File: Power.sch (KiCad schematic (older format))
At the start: 11 parts, among them P1 24 pin MiniFit JR, SW1 SWITCH_INV

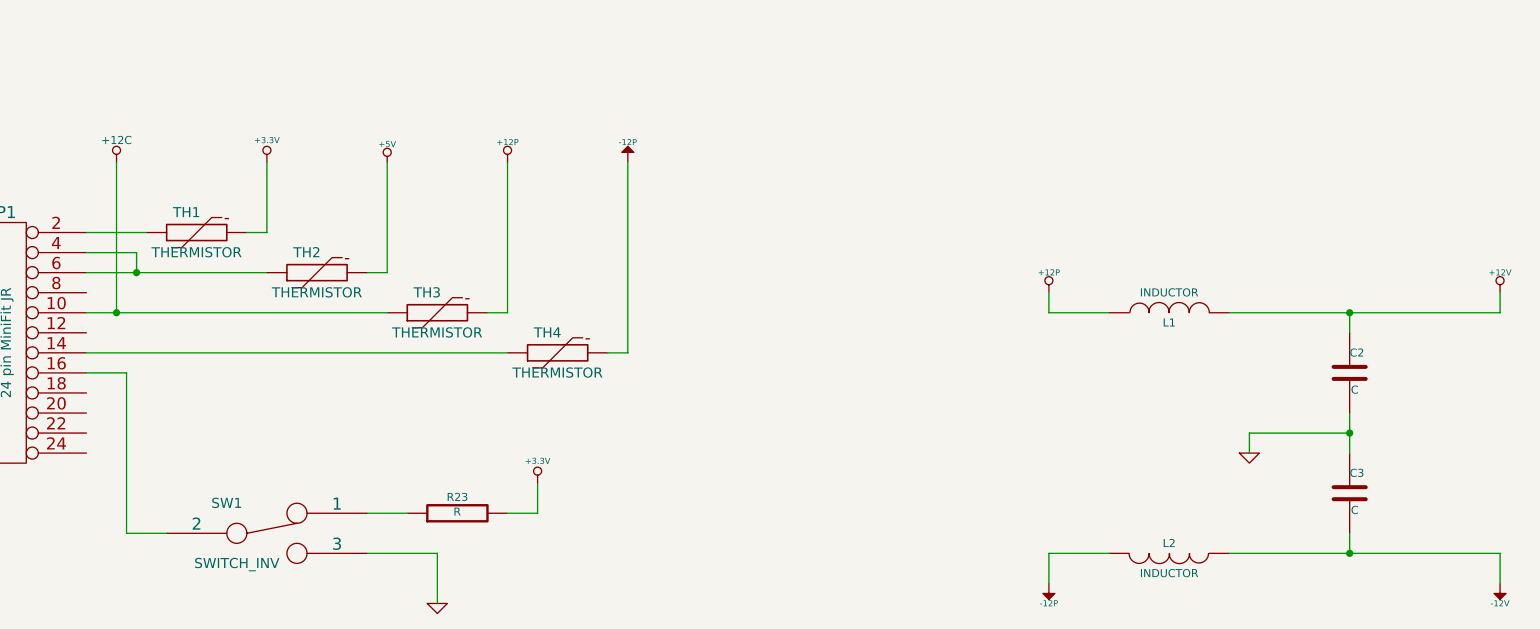
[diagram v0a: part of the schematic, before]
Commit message: Associating and Placing the Power Protection and Filtering Module
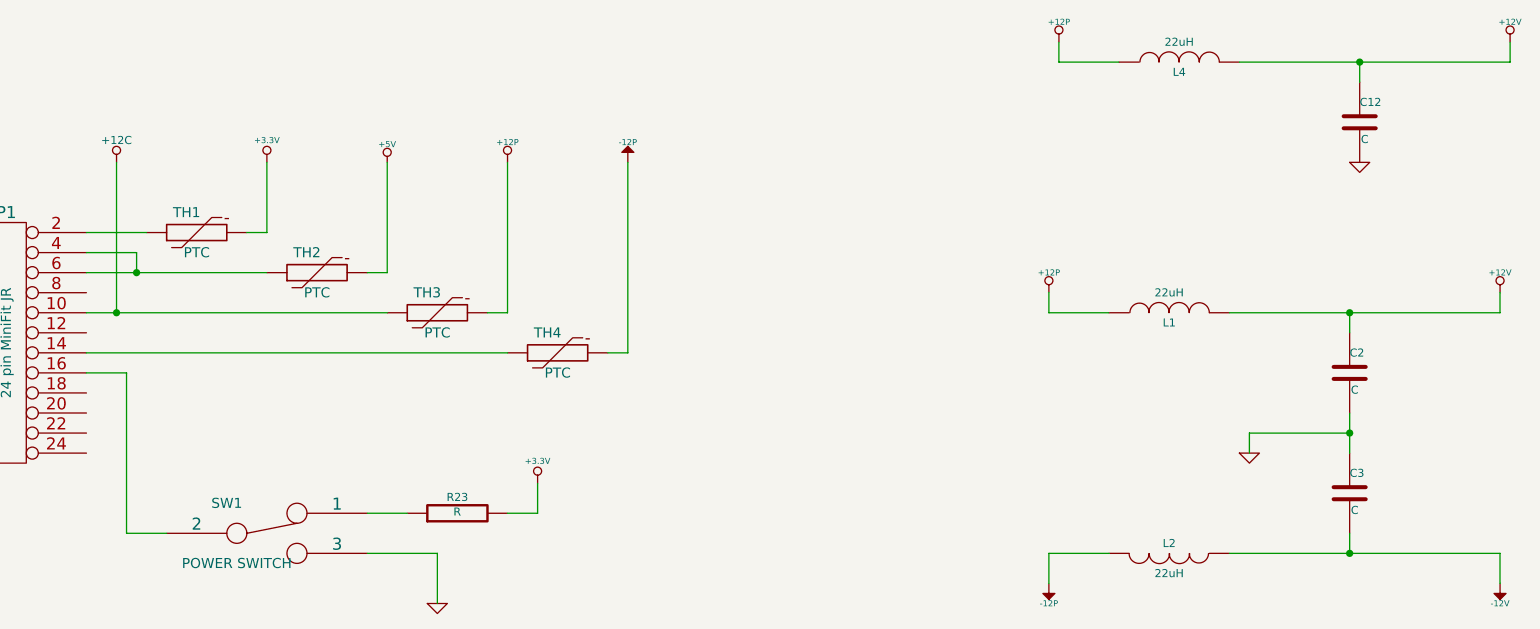
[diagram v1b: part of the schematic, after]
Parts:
- added C12: C, symbol C
- added L4: 22uH, symbol INDUCTOR
- L1, L2: value INDUCTOR -> 22uH; MFG Name (none) -> Bourns; MFG Part Number (none) -> CM322522-220KL
- SW1: value SWITCH_INV -> POWER SWITCH; MFG Name (none) -> C&K Components; MFG Part Number (none) -> OS102011MA1QN1
- TH1, TH2, TH3, TH4: value THERMISTOR -> PTC; MFG Name (none) -> TE Connectivity; MFG Part Number (none) -> MINISMDC050F-2
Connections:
- net +12P: now also L4.1
- net +12V: now also C12.1, L4.2
- net GND: now also C12.2
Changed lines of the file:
@@
 P 3700 3600
 F 0 "SW1" H 3500 3750 50  0000 C CNN
-F 1 "SWITCH_INV" H 3550 3450 50  0000 C CNN
+F 1 "POWER SWITCH" H 3550 3450 50  0000 C CNN
 F 2 "" H 3700 3600 60  0000 C CNN
 F 3 "" H 3700 3600 60  0000 C CNN
+F 4 "C&K Components" H 3700 3600 60  0001 C CNN "MFG Name"
+F 5 "OS102011MA1QN1" H 3700 3600 60  0001 C CNN "MFG Part Number"
 	1    3700 3600
 	1    0    0    -1
@@
 P 8200 2500
 F 0 "L1" V 8150 2500 40  0000 C CNN
-F 1 "INDUCTOR" V 8300 2500 40  0000 C CNN
+F 1 "22uH" V 8300 2500 40  0000 C CNN
 F 2 "" H 8200 2500 60  0000 C CNN
 F 3 "" H 8200 2500 60  0000 C CNN
+F 4 "Bourns" H 8200 2500 60  0001 C CNN "MFG Name"
+F 5 "CM322522-220KL" H 8200 2500 60  0001 C CNN "MFG Part Number"
 	1    8200 2500
 	0    -1   -1   0
@@
 P 8200 3700
 F 0 "L2" V 8150 3700 40  0000 C CNN
-F 1 "INDUCTOR" V 8300 3700 40  0000 C CNN
+F 1 "22uH" V 8300 3700 40  0000 C CNN
 F 2 "" H 8200 3700 60  0000 C CNN
 F 3 "" H 8200 3700 60  0000 C CNN
+F 4 "Bourns" H 8200 3700 60  0001 C CNN "MFG Name"
+F 5 "CM322522-220KL" H 8200 3700 60  0001 C CNN "MFG Part Number"
 	1    8200 3700
 	0    1    1    0
@@
 P 3350 2100
 F 0 "TH1" V 3450 2150 50  0000 C CNN
-F 1 "THERMISTOR" V 3250 2100 50  0000 C CNN
+F 1 "PTC" V 3250 2100 50  0000 C CNN
 F 2 "" H 3350 2100 60  0000 C CNN
 F 3 "" H 3350 2100 60  0000 C CNN
+F 4 "TE Connectivity" H 3350 2100 60  0001 C CNN "MFG Name"
+F 5 "MINISMDC050F-2" H 3350 2100 60  0001 C CNN "MFG Part Number"
 	1    3350 2100
 	0    -1   -1   0
@@
 P 3950 2300
 F 0 "TH2" V 4050 2350 50  0000 C CNN
-F 1 "THERMISTOR" V 3850 2300 50  0000 C CNN
+F 1 "PTC" V 3850 2300 50  0000 C CNN
 F 2 "" H 3950 2300 60  0000 C CNN
 F 3 "" H 3950 2300 60  0000 C CNN
+F 4 "TE Connectivity" H 3950 2300 60  0001 C CNN "MFG Name"
+F 5 "MINISMDC050F-2" H 3950 2300 60  0001 C CNN "MFG Part Number"
 	1    3950 2300
 	0    -1   -1   0
@@
 P 4550 2500
 F 0 "TH3" V 4650 2550 50  0000 C CNN
-F 1 "THERMISTOR" V 4450 2500 50  0000 C CNN
+F 1 "PTC" V 4450 2500 50  0000 C CNN
 F 2 "" H 4550 2500 60  0000 C CNN
 F 3 "" H 4550 2500 60  0000 C CNN
+F 4 "TE Connectivity" H 4550 2500 60  0001 C CNN "MFG Name"
+F 5 "MINISMDC050F-2" H 4550 2500 60  0001 C CNN "MFG Part Number"
 	1    4550 2500
 	0    -1   -1   0
@@
 P 5150 2700
 F 0 "TH4" V 5250 2750 50  0000 C CNN
-F 1 "THERMISTOR" V 5050 2700 50  0000 C CNN
+F 1 "PTC" V 5050 2700 50  0000 C CNN
 F 2 "" H 5150 2700 60  0000 C CNN
 F 3 "" H 5150 2700 60  0000 C CNN
+F 4 "TE Connectivity" H 5150 2700 60  0001 C CNN "MFG Name"
+F 5 "MINISMDC050F-2" H 5150 2700 60  0001 C CNN "MFG Part Number"
 	1    5150 2700
 	0    -1   -1   0
 $EndComp
+$Comp
+L +12P #PWR034
+U 1 1 530B10FD
+P 7650 1150
+F 0 "#PWR034" H 7650 1120 30  0001 C CNN
+F 1 "+12P" H 7650 1250 30  0000 C CNN
+F 2 "" H 7650 1150 60  0000 C CNN
+F 3 "" H 7650 1150 60  0000 C CNN
+	1    7650 1150
+	1    0    0    -1
+$EndComp
+$Comp
+L INDUCTOR L4
+U 1 1 530B1105
+P 8250 1250
+F 0 "L4" V 8200 1250 40  0000 C CNN
+F 1 "22uH" V 8350 1250 40  0000 C CNN
+F 2 "" H 8250 1250 60  0000 C CNN
+F 3 "" H 8250 1250 60  0000 C CNN
+F 4 "Bourns" H 8250 1250 60  0001 C CNN "MFG Name"
+F 5 "CM322522-220KL" H 8250 1250 60  0001 C CNN "MFG Part Number"
+	1    8250 1250
+	0    -1   -1   0
+$EndComp
+$Comp
+L C C12
+U 1 1 530B110B
+P 9150 1550
+F 0 "C12" H 9150 1650 40  0000 L CNN
+F 1 "C" H 9156 1465 40  0000 L CNN
+F 2 "" H 9188 1400 30  0000 C CNN
+F 3 "" H 9150 1550 60  0000 C CNN
+	1    9150 1550
+	1    0    0    -1
+$EndComp
+Wire Wire Line
+	9150 1350 9150 1250
+Wire Wire Line
+	8550 1250 9900 1250
+Wire Wire Line
+	7650 1150 7650 1250
+Wire Wire Line
+	7650 1250 7950 1250
+$Comp
+L +12V #PWR035
+U 1 1 530B1115
+P 9900 1150
+F 0 "#PWR035" H 9900 1100 20  0001 C CNN
+F 1 "+12V" H 9900 1250 30  0000 C CNN
+F 2 "" H 9900 1150 60  0000 C CNN
+F 3 "" H 9900 1150 60  0000 C CNN
+	1    9900 1150
+	1    0    0    -1
+$EndComp
+Wire Wire Line
+	9900 1250 9900 1150
+Connection ~ 9150 1250
+$Comp
+L GND #PWR036
+U 1 1 530B111D
+P 9150 1750
+F 0 "#PWR036" H 9150 1750 30  0001 C CNN
+F 1 "GND" H 9150 1680 30  0001 C CNN
+F 2 "" H 9150 1750 60  0000 C CNN
+F 3 "" H 9150 1750 60  0000 C CNN
+	1    9150 1750
+	1    0    0    -1
+$EndComp
 $EndSCHEMATC

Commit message: Merge CE BenchBudEE commit 00937c39d96b9ebb1b0292c11cc231788ab24edd
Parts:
- removed C12: C, symbol C
- removed L4: 22uH, symbol INDUCTOR
- removed R23: R, symbol R
- added C4: C, ~, symbol C
- added L3: CM322522-220KL, ~, symbol INDUCTOR
- added R14: R, ~, symbol R
- C2, C3: footprint (none) -> ~
- L1, L2: value 22uH -> CM322522-220KL; footprint (none) -> ~; MFG Name Bourns -> Bournes
- P1: value 24 pin MiniFit JR -> 24 Pin MiniFit JR
- SW1: value POWER SWITCH -> Power Switch; footprint (none) -> ~
- TH1, TH2, TH3, TH4: value PTC -> MINISMDC050F-2; footprint (none) -> ~
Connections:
- net +12P: now also L3.1; no longer L1.1
- net +12V: now also C3.1, L3.2; no longer C2.1, L1.2
- net +3.3V: now also R14.2
- net +5V: now also C2.1, L1.2; no longer TH2.2
- net -12V: now also C4.2; no longer C3.2
- net GND: now also C3.2, C4.1; no longer C3.1
- net at P1.12 (P12): now also P1.2 (P2), TH1.1
- net at SW1.1: now also R14.1
- new net +5P: L1.1, TH2.2

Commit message: Layout Work Session 6
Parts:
- added TP1: CONN_1, symbol CONN_1
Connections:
- net GND: now also TP1.1
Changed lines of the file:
@@
 $EndComp
 $Comp
-L GND #PWR045
+L GND #PWR046
 U 1 1 523DFA76
 P 1400 1850
-F 0 "#PWR045" H 1400 1850 30  0001 C CNN
+F 0 "#PWR046" H 1400 1850 30  0001 C CNN
 F 1 "GND" H 1400 1780 30  0001 C CNN
 F 2 "" H 1400 1850 60  0000 C CNN
@@
 	5500 1900 5500 1150
 $Comp
-L +12P #PWR046
+L +12P #PWR047
 U 1 1 523DFB91
 P 5500 1150
-F 0 "#PWR046" H 5500 1120 30  0001 C CNN
+F 0 "#PWR047" H 5500 1120 30  0001 C CNN
 F 1 "+12P" H 5500 1250 30  0000 C CNN
 F 2 "" H 5500 1150 60  0000 C CNN
@@
 $EndComp
 $Comp
-L -12P #PWR047
+L -12P #PWR048
 U 1 1 523E04D8
 P 6100 1150
-F 0 "#PWR047" H 6100 1280 20  0001 C CNN
+F 0 "#PWR048" H 6100 1280 20  0001 C CNN
 F 1 "-12P" H 6100 1250 30  0000 C CNN
 F 2 "" H 6100 1150 60  0000 C CNN
@@
 	4800 3200 4800 3450
 $Comp
-L GND #PWR048
+L GND #PWR049
 U 1 1 523E08C4
 P 4800 3450
-F 0 "#PWR048" H 4800 3450 30  0001 C CNN
+F 0 "#PWR049" H 4800 3450 30  0001 C CNN
 F 1 "GND" H 4800 3380 30  0001 C CNN
 F 2 "" H 4800 3450 60  0000 C CNN
@@
 	5650 3000 5650 2750
 $Comp
-L +3.3V #PWR049
+L +3.3V #PWR050
 U 1 1 523E0910
 P 5650 2750
-F 0 "#PWR049" H 5650 2710 30  0001 C CNN
+F 0 "#PWR050" H 5650 2710 30  0001 C CNN
 F 1 "+3.3V" H 5650 2860 30  0000 C CNN
 F 2 "" H 5650 2750 60  0000 C CNN
@@
 $EndComp
 $Comp
-L +12P #PWR050
+L +12P #PWR051
 U 1 1 523E0C76
 P 8000 2250
-F 0 "#PWR050" H 8000 2220 30  0001 C CNN
+F 0 "#PWR051" H 8000 2220 30  0001 C CNN
 F 1 "+12P" H 8000 2350 30  0000 C CNN
 F 2 "" H 8000 2250 60  0000 C CNN
@@
 $EndComp
 $Comp
-L -12P #PWR051
+L -12P #PWR052
 U 1 1 523E0C7C
 P 8000 3800
-F 0 "#PWR051" H 8000 3930 20  0001 C CNN
+F 0 "#PWR052" H 8000 3930 20  0001 C CNN
 F 1 "-12P" H 8000 3900 30  0000 C CNN
 F 2 "" H 8000 3800 60  0000 C CNN
@@
 $EndComp
 $Comp
-L GND #PWR052
+L GND #PWR053
 U 1 1 523E0C82
 P 9000 3200
-F 0 "#PWR052" H 9000 3200 30  0001 C CNN
+F 0 "#PWR053" H 9000 3200 30  0001 C CNN
 F 1 "GND" H 9000 3130 30  0001 C CNN
 F 2 "" H 9000 3200 60  0000 C CNN
@@
 Connection ~ 9450 3050
 $Comp
-L -12V #PWR053
+L -12V #PWR054
 U 1 1 523E0DD3
 P 10350 3800
-F 0 "#PWR053" H 10350 3930 20  0001 C CNN
+F 0 "#PWR054" H 10350 3930 20  0001 C CNN
 F 1 "-12V" H 10350 3900 30  0000 C CNN
 F 2 "" H 10350 3800 60  0000 C CNN
@@
 Connection ~ 9450 2450
 $Comp
-L +12V #PWR054
+L +12V #PWR055
 U 1 1 523E0E37
 P 10350 2200
-F 0 "#PWR054" H 10350 2150 20  0001 C CNN
+F 0 "#PWR055" H 10350 2150 20  0001 C CNN
 F 1 "+12V" H 10350 2300 30  0000 C CNN
 F 2 "" H 10350 2200 60  0000 C CNN
@@
 Connection ~ 3450 1900
 $Comp
-L +12C #PWR055
+L +12C #PWR056
 U 1 1 52438F0D
 P 3450 1150
-F 0 "#PWR055" H 3450 1120 30  0001 C CNN
+F 0 "#PWR056" H 3450 1120 30  0001 C CNN
 F 1 "+12C" H 3450 1260 40  0000 C CNN
 F 2 "~" H 3450 1150 60  0000 C CNN
@@
 $EndComp
 $Comp
-L GND #PWR056
+L GND #PWR057
 U 1 1 524502FC
 P 9400 1650
-F 0 "#PWR056" H 9400 1650 30  0001 C CNN
+F 0 "#PWR057" H 9400 1650 30  0001 C CNN
 F 1 "GND" H 9400 1580 30  0001 C CNN
 F 2 "" H 9400 1650 60  0000 C CNN
@@
 $EndComp
 $Comp
-L +5V #PWR057
+L +5V #PWR058
 U 1 1 524503B6
 P 10300 650
-F 0 "#PWR057" H 10300 740 20  0001 C CNN
+F 0 "#PWR058" H 10300 740 20  0001 C CNN
 F 1 "+5V" H 10300 740 30  0000 C CNN
 F 2 "~" H 10300 650 60  0000 C CNN
@@
 $EndComp
 $Comp
-L +3.3V #PWR058
+L +3.3V #PWR059
 U 1 1 526E168C
 P 4400 1150
-F 0 "#PWR058" H 4400 1110 30  0001 C CNN
+F 0 "#PWR059" H 4400 1110 30  0001 C CNN
 F 1 "+3.3V" H 4400 1260 30  0000 C CNN
 F 2 "" H 4400 1150 60  0000 C CNN
@@
 	3550 2000 3550 1500
 Connection ~ 3550 1500
+$Comp
+L CONN_1 TP1
+U 1 1 53148E2B
+P 6775 4025
+F 0 "TP1" H 6855 4025 40  0000 L CNN
+F 1 "CONN_1" H 6775 4080 30  0001 C CNN
+F 2 "" H 6775 4025 60  0000 C CNN
+F 3 "" H 6775 4025 60  0000 C CNN
+	1    6775 4025
+	-1   0    0    1
+$EndComp
+$Comp
+L GND #PWR060
+U 1 1 53148E56
+P 7100 4125
+F 0 "#PWR060" H 7100 4125 30  0001 C CNN
+F 1 "GND" H 7100 4055 30  0001 C CNN
+F 2 "" H 7100 4125 60  0000 C CNN
+F 3 "" H 7100 4125 60  0000 C CNN
+	1    7100 4125
+	1    0    0    -1
+$EndComp
+Wire Wire Line
+	7100 4125 7100 4025
+Wire Wire Line
+	7100 4025 6925 4025
 $EndSCHEMATC

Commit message: Layout Work Session 6
Pulled from CE
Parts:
- added JP1, JP2, JP3, JP4: JUMPER, ~, symbol JUMPER
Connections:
- net GND: now also JP1.1, JP2.1, JP3.1, JP4.1
- new net AGND: JP1.2
- new net GND_LED: JP3.2
- new net GND_PWR: JP2.2
- new net GND_RELAY: JP4.2
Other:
- note added: "Star Point"
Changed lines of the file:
@@
-EESchema Schematic File Version 2
+EESchema Schematic File Version 2  date 11/10/2013 9:27:17 PM
 LIBS:power
 LIBS:device
@@
 LIBS:valves
 LIBS:BenchBuddy
-LIBS:arduino_shieldsNCL
 LIBS:BenchBuddy-cache
-EELAYER 24 0
+EELAYER 27 0
 EELAYER END
 $Descr A4 11693 8268
@@
 Sheet 9 9
 Title ""
-Date "2 nov 2013"
+Date "11 nov 2013"
 Rev ""
 Comp ""
@@
 $EndComp
 $Comp
-L GND #PWR046
+L GND #PWR51
 U 1 1 523DFA76
 P 1400 1850
-F 0 "#PWR046" H 1400 1850 30  0001 C CNN
+F 0 "#PWR51" H 1400 1850 30  0001 C CNN
 F 1 "GND" H 1400 1780 30  0001 C CNN
 F 2 "" H 1400 1850 60  0000 C CNN
@@
 	5500 1900 5500 1150
 $Comp
-L +12P #PWR047
+L +12P #PWR57
 U 1 1 523DFB91
 P 5500 1150
-F 0 "#PWR047" H 5500 1120 30  0001 C CNN
+F 0 "#PWR57" H 5500 1120 30  0001 C CNN
 F 1 "+12P" H 5500 1250 30  0000 C CNN
 F 2 "" H 5500 1150 60  0000 C CNN
@@
 $EndComp
 $Comp
-L -12P #PWR048
+L -12P #PWR59
 U 1 1 523E04D8
 P 6100 1150
-F 0 "#PWR048" H 6100 1280 20  0001 C CNN
+F 0 "#PWR59" H 6100 1280 20  0001 C CNN
 F 1 "-12P" H 6100 1250 30  0000 C CNN
 F 2 "" H 6100 1150 60  0000 C CNN
@@
 	4800 3200 4800 3450
 $Comp
-L GND #PWR049
+L GND #PWR54
 U 1 1 523E08C4
 P 4800 3450
-F 0 "#PWR049" H 4800 3450 30  0001 C CNN
+F 0 "#PWR54" H 4800 3450 30  0001 C CNN
 F 1 "GND" H 4800 3380 30  0001 C CNN
 F 2 "" H 4800 3450 60  0000 C CNN
@@
 	5650 3000 5650 2750
 $Comp
-L +3.3V #PWR050
+L +3.3V #PWR58
 U 1 1 523E0910
 P 5650 2750
-F 0 "#PWR050" H 5650 2710 30  0001 C CNN
+F 0 "#PWR58" H 5650 2710 30  0001 C CNN
 F 1 "+3.3V" H 5650 2860 30  0000 C CNN
 F 2 "" H 5650 2750 60  0000 C CNN
@@
 $EndComp
 $Comp
-L +12P #PWR051
+L +12P #PWR66
 U 1 1 523E0C76
 P 8000 2250
-F 0 "#PWR051" H 8000 2220 30  0001 C CNN
+F 0 "#PWR66" H 8000 2220 30  0001 C CNN
 F 1 "+12P" H 8000 2350 30  0000 C CNN
 F 2 "" H 8000 2250 60  0000 C CNN
@@
 $EndComp
 $Comp
-L -12P #PWR052
+L -12P #PWR67
 U 1 1 523E0C7C
 P 8000 3800
-F 0 "#PWR052" H 8000 3930 20  0001 C CNN
+F 0 "#PWR67" H 8000 3930 20  0001 C CNN
 F 1 "-12P" H 8000 3900 30  0000 C CNN
 F 2 "" H 8000 3800 60  0000 C CNN
@@
 $EndComp
 $Comp
-L GND #PWR053
+L GND #PWR68
 U 1 1 523E0C82
 P 9000 3200
-F 0 "#PWR053" H 9000 3200 30  0001 C CNN
+F 0 "#PWR68" H 9000 3200 30  0001 C CNN
 F 1 "GND" H 9000 3130 30  0001 C CNN
 F 2 "" H 9000 3200 60  0000 C CNN
@@
 Connection ~ 9450 3050
 $Comp
-L -12V #PWR054
+L -12V #PWR72
 U 1 1 523E0DD3
 P 10350 3800
-F 0 "#PWR054" H 10350 3930 20  0001 C CNN
+F 0 "#PWR72" H 10350 3930 20  0001 C CNN
 F 1 "-12V" H 10350 3900 30  0000 C CNN
 F 2 "" H 10350 3800 60  0000 C CNN
@@
 Connection ~ 9450 2450
 $Comp
-L +12V #PWR055
+L +12V #PWR71
 U 1 1 523E0E37
 P 10350 2200
-F 0 "#PWR055" H 10350 2150 20  0001 C CNN
+F 0 "#PWR71" H 10350 2150 20  0001 C CNN
 F 1 "+12V" H 10350 2300 30  0000 C CNN
 F 2 "" H 10350 2200 60  0000 C CNN
@@
 Connection ~ 3450 1900
 $Comp
-L +12C #PWR056
+L +12C #PWR52
 U 1 1 52438F0D
 P 3450 1150
-F 0 "#PWR056" H 3450 1120 30  0001 C CNN
+F 0 "#PWR52" H 3450 1120 30  0001 C CNN
 F 1 "+12C" H 3450 1260 40  0000 C CNN
 F 2 "~" H 3450 1150 60  0000 C CNN
@@
 $EndComp
 $Comp
-L GND #PWR057
+L GND #PWR69
 U 1 1 524502FC
 P 9400 1650
-F 0 "#PWR057" H 9400 1650 30  0001 C CNN
+F 0 "#PWR69" H 9400 1650 30  0001 C CNN
 F 1 "GND" H 9400 1580 30  0001 C CNN
 F 2 "" H 9400 1650 60  0000 C CNN
@@
 Connection ~ 9400 900
 $Comp
-L +5P #PWR58
+L +5P #PWR56
 U 1 1 52450355
 P 4900 1150
-F 0 "#PWR58" H 4900 1280 20  0001 C CNN
+F 0 "#PWR56" H 4900 1280 20  0001 C CNN
 F 1 "+5P" H 4900 1250 30  0000 C CNN
 F 2 "~" H 4900 1150 60  0000 C CNN
@@
 $EndComp
 $Comp
-L +5P #PWR62
+L +5P #PWR65
 U 1 1 52450371
 P 7950 700
-F 0 "#PWR62" H 7950 830 20  0001 C CNN
+F 0 "#PWR65" H 7950 830 20  0001 C CNN
 F 1 "+5P" H 7950 800 30  0000 C CNN
 F 2 "~" H 7950 700 60  0000 C CNN
@@
 $EndComp
 $Comp
-L +5V #PWR058
+L +5V #PWR70
 U 1 1 524503B6
 P 10300 650
-F 0 "#PWR058" H 10300 740 20  0001 C CNN
+F 0 "#PWR70" H 10300 740 20  0001 C CNN
 F 1 "+5V" H 10300 740 30  0000 C CNN
 F 2 "~" H 10300 650 60  0000 C CNN
@@
 $EndComp
 $Comp
-L +3.3V #PWR059
+L +3.3V #PWR53
 U 1 1 526E168C
 P 4400 1150
-F 0 "#PWR059" H 4400 1110 30  0001 C CNN
+F 0 "#PWR53" H 4400 1110 30  0001 C CNN
 F 1 "+3.3V" H 4400 1260 30  0000 C CNN
 F 2 "" H 4400 1150 60  0000 C CNN
@@
 $Comp
 L CONN_1 TP1
-U 1 1 53148E2B
-P 6775 4025
-F 0 "TP1" H 6855 4025 40  0000 L CNN
-F 1 "CONN_1" H 6775 4080 30  0001 C CNN
-F 2 "" H 6775 4025 60  0000 C CNN
-F 3 "" H 6775 4025 60  0000 C CNN
-	1    6775 4025
+U 1 1 527EFE16
+P 5800 5400
+F 0 "TP1" H 5880 5400 40  0000 L CNN
+F 1 "CONN_1" H 5800 5455 30  0001 C CNN
+F 2 "" H 5800 5400 60  0000 C CNN
+F 3 "" H 5800 5400 60  0000 C CNN
+	1    5800 5400
 	-1   0    0    1
 $EndComp
 $Comp
-L GND #PWR060
-U 1 1 53148E56
-P 7100 4125
-F 0 "#PWR060" H 7100 4125 30  0001 C CNN
-F 1 "GND" H 7100 4055 30  0001 C CNN
-F 2 "" H 7100 4125 60  0000 C CNN
-F 3 "" H 7100 4125 60  0000 C CNN
-	1    7100 4125
-	1    0    0    -1
-$EndComp
-Wire Wire Line
-	7100 4125 7100 4025
-Wire Wire Line
-	7100 4025 6925 4025
+L GND #PWR60
+U 1 1 527EFE6B
+P 6100 5550
+F 0 "#PWR60" H 6100 5550 30  0001 C CNN
+F 1 "GND" H 6100 5480 30  0001 C CNN
+F 2 "" H 6100 5550 60  0000 C CNN
+F 3 "" H 6100 5550 60  0000 C CNN
+	1    6100 5550
+	1    0    0    -1
+$EndComp
+Wire Wire Line
+	6100 5550 6100 5400
+Wire Wire Line
+	6100 5400 5950 5400
+Text Notes 5100 5400 0    60   ~ 0
+Star Point
+$Comp
+L JUMPER JP1
+U 1 1 52804A88
+P 5450 6050
+F 0 "JP1" H 5450 6200 60  0000 C CNN
+F 1 "JUMPER" H 5450 5970 40  0000 C CNN
+F 2 "~" H 5450 6050 60  0000 C CNN
+F 3 "~" H 5450 6050 60  0000 C CNN
+	1    5450 6050
+	1    0    0    -1
+$EndComp
+$Comp
+L JUMPER JP2
+U 1 1 52804A95
+P 5450 6450
+F 0 "JP2" H 5450 6600 60  0000 C CNN
+F 1 "JUMPER" H 5450 6370 40  0000 C CNN
+F 2 "~" H 5450 6450 60  0000 C CNN
+F 3 "~" H 5450 6450 60  0000 C CNN
+	1    5450 6450
+	1    0    0    -1
+$EndComp
+$Comp
+L JUMPER JP3
+U 1 1 52804A9B
+P 5450 6800
+F 0 "JP3" H 5450 6950 60  0000 C CNN
+F 1 "JUMPER" H 5450 6720 40  0000 C CNN
+F 2 "~" H 5450 6800 60  0000 C CNN
+F 3 "~" H 5450 6800 60  0000 C CNN
+	1    5450 6800
+	1    0    0    -1
+$EndComp
+$Comp
+L JUMPER JP4
+U 1 1 52804AA1
+P 5450 7150
+F 0 "JP4" H 5450 7300 60  0000 C CNN
+F 1 "JUMPER" H 5450 7070 40  0000 C CNN
+F 2 "~" H 5450 7150 60  0000 C CNN
+F 3 "~" H 5450 7150 60  0000 C CNN
+	1    5450 7150
+	1    0    0    -1
+$EndComp
+$Comp
+L GND #PWR55
+U 1 1 52804AA7
+P 4800 7450
+F 0 "#PWR55" H 4800 7450 30  0001 C CNN
+F 1 "GND" H 4800 7380 30  0001 C CNN
+F 2 "" H 4800 7450 60  0000 C CNN
+F 3 "" H 4800 7450 60  0000 C CNN
+	1    4800 7450
+	1    0    0    -1
+$EndComp
+Wire Wire Line
+	4800 7450 4800 6050
+Wire Wire Line
+	4800 6050 5150 6050
+Wire Wire Line
+	4800 6450 5150 6450
+Connection ~ 4800 6450
+Wire Wire Line
+	5150 6800 4800 6800
+Connection ~ 4800 6800
+Wire Wire Line
+	5150 7150 4800 7150
+Connection ~ 4800 7150
+Wire Wire Line
+	5750 6050 6200 6050
+$Comp
+L GND_RELAY #PWR64
+U 1 1 52804C2C
+P 6200 7400
+F 0 "#PWR64" H 6200 7400 30  0001 C CNN
+F 1 "GND_RELAY" H 6200 7330 30  0000 C CNN
+F 2 "~" H 6200 7400 60  0000 C CNN
+F 3 "~" H 6200 7400 60  0000 C CNN
+	1    6200 7400
+	1    0    0    -1
+$EndComp
+$Comp
+L GND_LED #PWR63
+U 1 1 52804C3B
+P 6200 6950
+F 0 "#PWR63" H 6200 6950 30  0001 C CNN
+F 1 "GND_LED" H 6200 6880 30  0000 C CNN
+F 2 "~" H 6200 6950 60  0000 C CNN
+F 3 "~" H 6200 6950 60  0000 C CNN
+	1    6200 6950
+	1    0    0    -1
+$EndComp
+$Comp
+L GND_PWR #PWR62
+U 1 1 52804C4A
+P 6200 6550
+F 0 "#PWR62" H 6200 6550 30  0001 C CNN
+F 1 "GND_PWR" H 6200 6480 30  0000 C CNN
+F 2 "~" H 6200 6550 60  0000 C CNN
+F 3 "~" H 6200 6550 60  0000 C CNN
+	1    6200 6550
+	1    0    0    -1
+$EndComp
+$Comp
+L AGND #PWR61
+U 1 1 52804C59
+P 6200 6200
+F 0 "#PWR61" H 6200 6200 40  0001 C CNN
+F 1 "AGND" H 6200 6130 50  0000 C CNN
+F 2 "~" H 6200 6200 60  0000 C CNN
+F 3 "~" H 6200 6200 60  0000 C CNN
+	1    6200 6200
+	1    0    0    -1
+$EndComp
+Wire Wire Line
+	6200 6050 6200 6200
+Wire Wire Line
+	6200 6550 6200 6450
+Wire Wire Line
+	6200 6450 5750 6450
+Wire Wire Line
+	5750 6800 6200 6800
+Wire Wire Line
+	6200 6800 6200 6950
+Wire Wire Line
+	6200 7400 6200 7150
+Wire Wire Line
+	6200 7150 5750 7150
 $EndSCHEMATC
